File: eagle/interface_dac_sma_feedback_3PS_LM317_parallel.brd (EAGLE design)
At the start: 95.6 x 144.9 mm, 38 parts, among them IC1 ISO1540, X1 BU-SMA-V

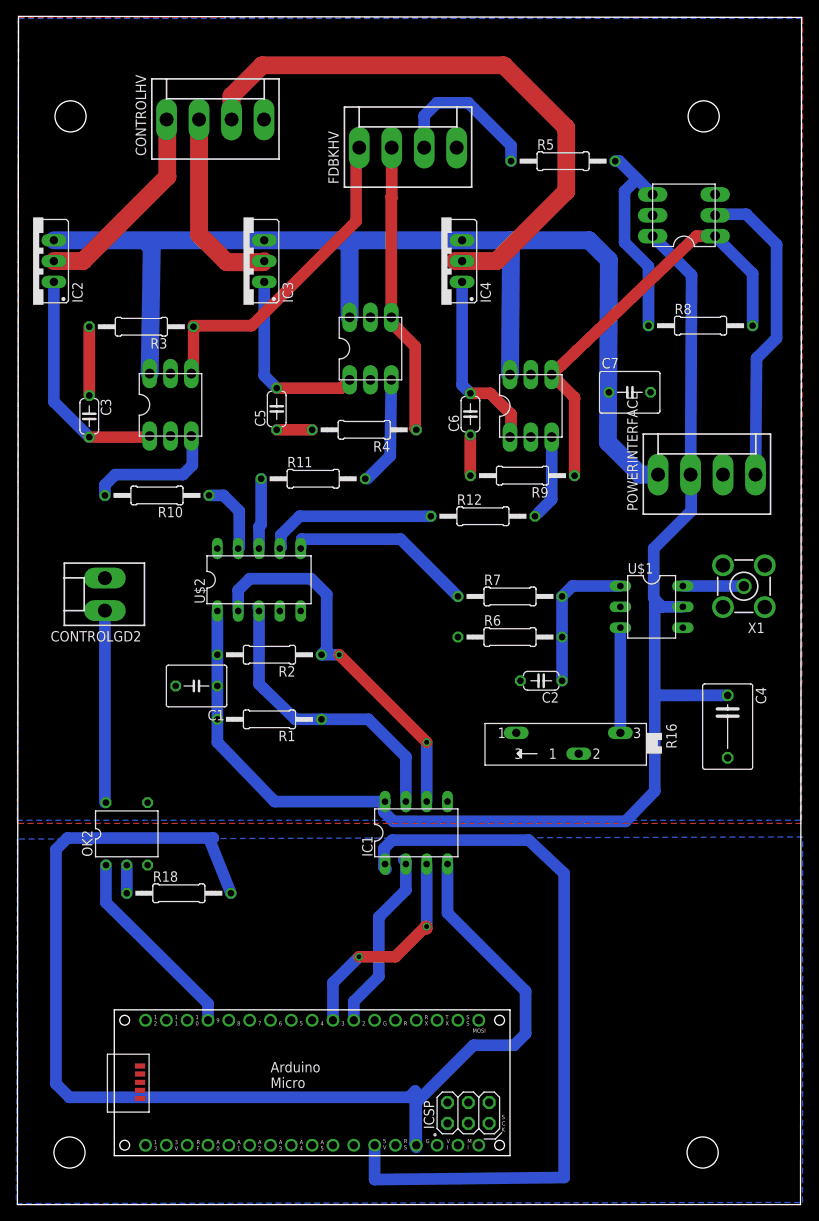
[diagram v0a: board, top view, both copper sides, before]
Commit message: two ps in parallel
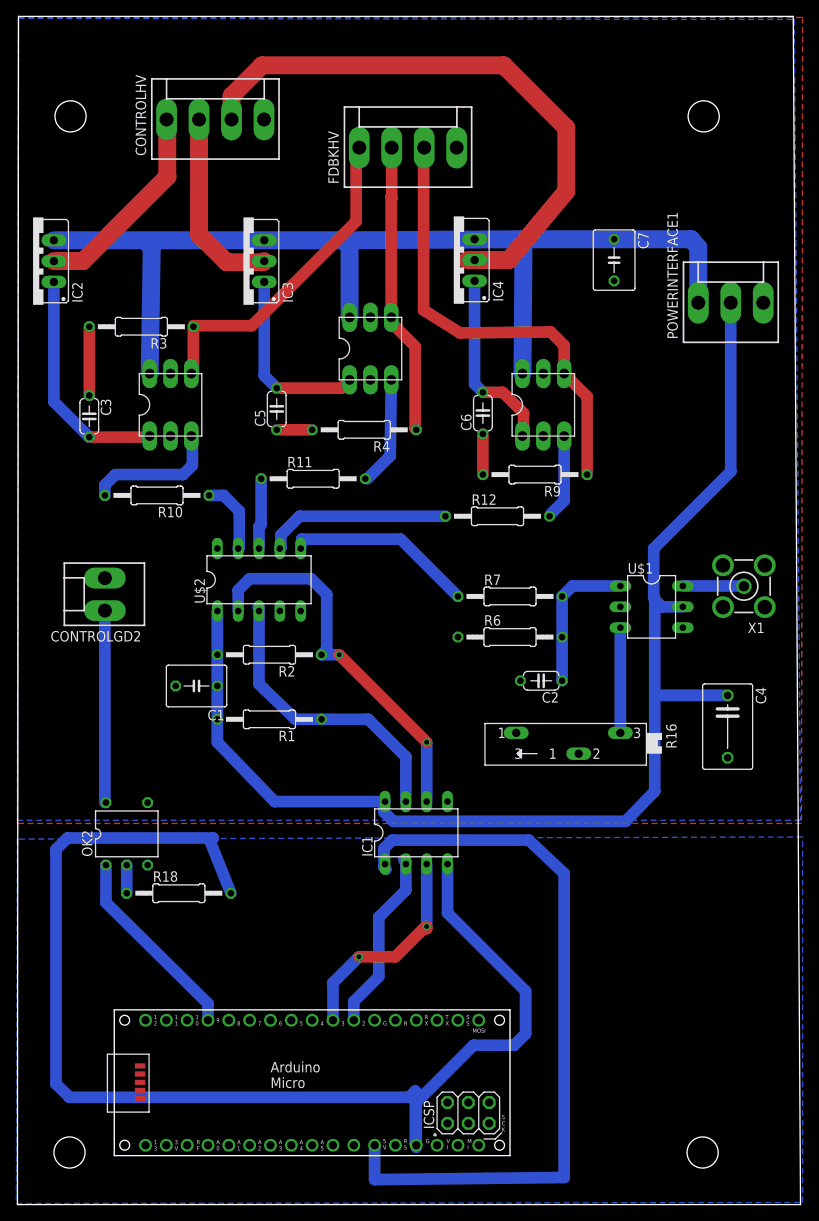
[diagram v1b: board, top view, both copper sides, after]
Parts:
- removed POWERINTERFACE: (no value), con-molex:KK-156-4
- removed R5, R8: 20k, resistor:0207/12
- removed U$3: OPA735DIL, texas:DIL6
- added POWERINTERFACE1: (no value), con-molex:KK-156-3
- R12: value 12 -> 20k
- moved C7 16.2 mm to (72.8, 115.2), turned to 270 degrees
- moved R12 1.78 mm to (58.5, 83.9)
- moved U$4 1.53 mm to (64.1, 97.5)
- moved C6 1.53 mm to (56.8, 96.5)
- moved IC4 1.53 mm to (53.2, 115.2)
- moved R9 1.53 mm to (63.1, 89.0)
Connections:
- removed net -5V: POWERINTERFACE.4, U$3.P$2
- removed net N$23: R5.2, R8.1, U$3.P$4
- removed net N$9: FDBKHV.3, R5.1
- net +12V: now also POWERINTERFACE1.1; no longer POWERINTERFACE.1
- net GND: now also POWERINTERFACE1.3; no longer POWERINTERFACE.3, U$3.P$3
- net N$14: now also FDBKHV.3; no longer R8.2, U$3.P$1
- net VCC: now also POWERINTERFACE1.2; no longer POWERINTERFACE.2, U$3.P$6
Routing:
- net -5V: track 38.2 -> 0.00 mm
- net N$23: track 26.0 -> 0.00 mm
- net N$9: track 19.2 -> 0.00 mm
- net +12V: track 140.7 -> 127.8 mm
- net VCC: track 160.2 -> 152.1 mm
- net N$14: track 53.0 -> 55.4 mm
- net N$25: track 20.9 -> 22.7 mm
- net N$5: track 73.3 -> 72.1 mm
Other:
- board size 95.6 x 144.9 mm -> 95.5 x 144.9 mm
